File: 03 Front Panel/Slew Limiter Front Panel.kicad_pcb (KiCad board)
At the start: 2 copper layers, 20 x 128.3 mm, 1 part

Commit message: Update to v1.2
Many changes, see readme for list
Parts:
- removed the G*** at (150.5, -117.0)
- added G***: LOGO, graphics:Slew Limiter Front Panel Graphics, F.Cu at (0.00, -8.00)
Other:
- board size 20 x 128.3 mm -> 20 x 128 mm
- board text added: "JLCJLCJLCJLC"

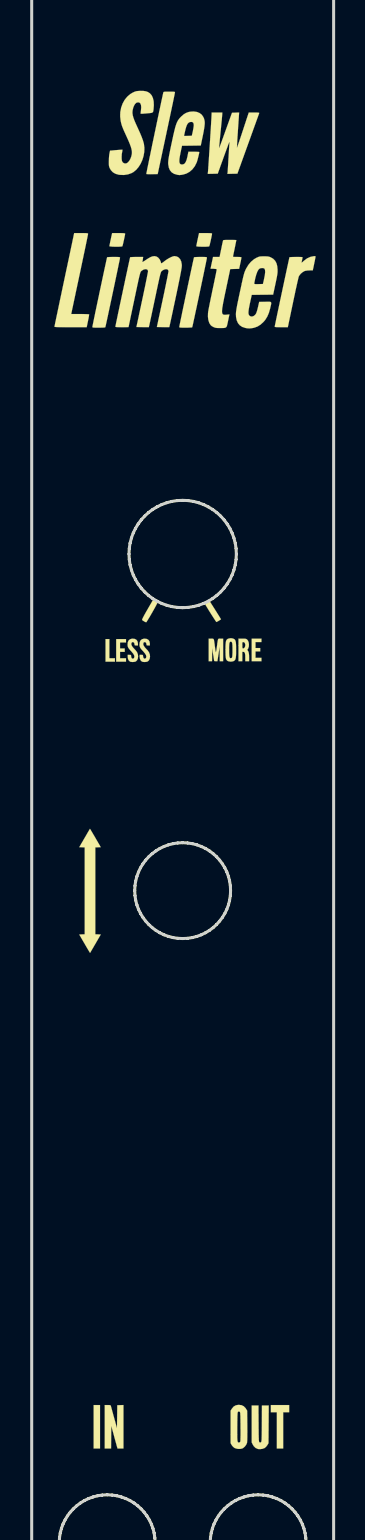
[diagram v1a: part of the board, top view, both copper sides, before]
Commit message: Front panel text fix
Nudge input and output text
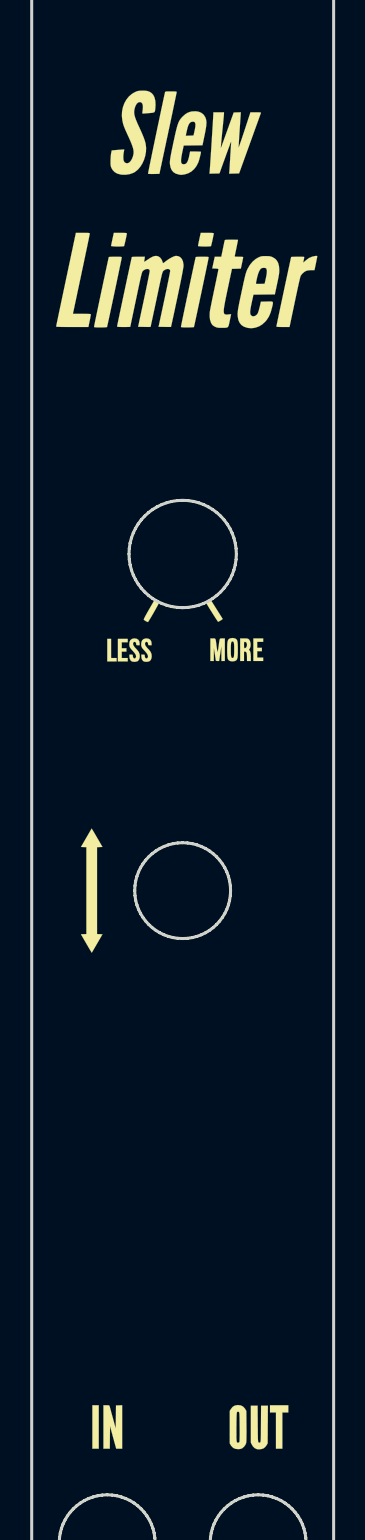
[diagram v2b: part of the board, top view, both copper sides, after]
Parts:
- moved G*** 8.00 mm to (0.00, 0.00)
